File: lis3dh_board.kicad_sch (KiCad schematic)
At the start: 11 parts, among them J1 T4_I2C2, J2 BQ25798_BOARD, U1 TLV75530PDBV, U2 LIS3DH

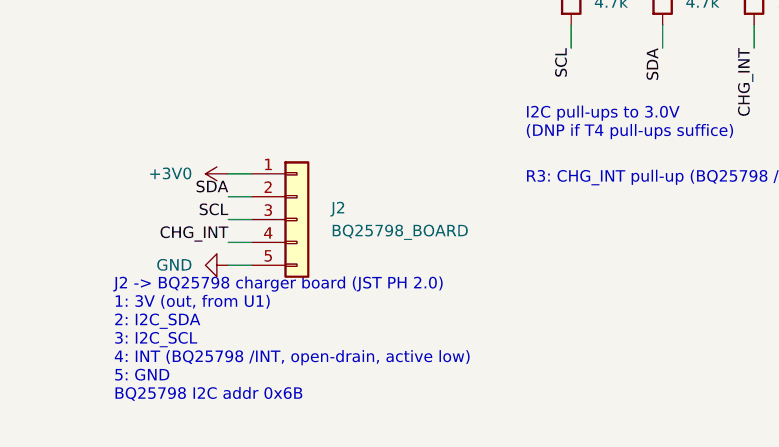
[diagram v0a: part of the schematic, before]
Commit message: Reverse J2 pin order for the charger board connector
J2 (JST PH 2.0 to the BQ25798 board) is now 1 GND, 2 INT, 3 SCL,
4 SDA, 5 3V. Nets are unchanged; only the pin numbering is reversed.

Co-Authored-By: Claude Opus 5.5 <noreply@anthropic.com>
Claude-Session: https://claude.ai/code/session_012K15v8QNdkAoa4NiCNiWuG
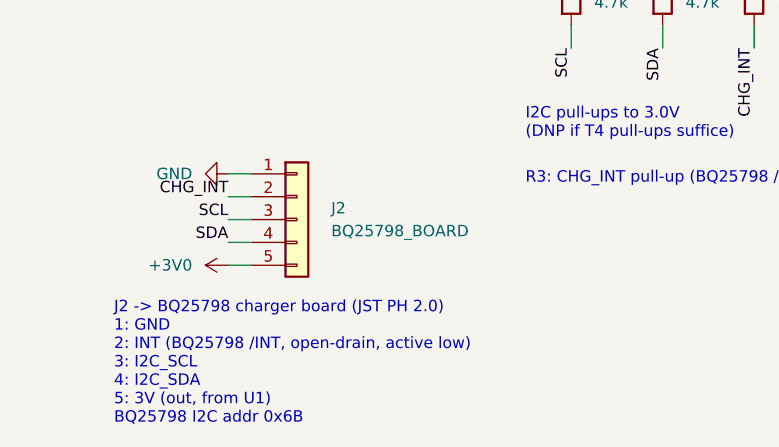
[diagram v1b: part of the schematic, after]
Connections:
- net +3V0: now also J2.5 (Pin_5); no longer J2.1 (Pin_1)
- net CHG_INT: now also J2.2 (Pin_2); no longer J2.4 (Pin_4)
- net GND: now also J2.1 (Pin_1); no longer J2.5 (Pin_5)
- net SDA: now also J2.4 (Pin_4); no longer J2.2 (Pin_2)
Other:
- note added: "J2 -> BQ25798 charger board (JST PH 2.0) 1: GND 2: INT (BQ25798 /INT, open-drain, active low) 3: I2C_SCL 4: I2C_SDA 5: 3V (out, from U1) BQ25798 I2C addr 0x6B"
- note removed: "J2 -> BQ25798 charger board (JST PH 2.0) 1: 3V (out, from U1) 2: I2C_SDA 3: I2C_SCL 4: INT (BQ25798 /INT, open-drain, active low) 5: GND BQ25798 I2C addr 0x6B"
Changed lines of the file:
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@@
     (stroke (width 0) (type default))
   )
-  (symbol (lib_id "power:+3V0") (at 43.18 137.16 90) (unit 1)
+  (symbol (lib_id "power:GND") (at 43.18 137.16 270) (unit 1)
     (in_bom no) (on_board no) (dnp no)
     (property "Reference" "#PWR016" (at 43.18 143.16 0)
       (effects (font (size 1.27 1.27)) hide)
     )
-    (property "Value" "+3V0" (at 39.18 137.16 90)
+    (property "Value" "GND" (at 39.18 137.16 270)
       (effects (font (size 1.27 1.27)) (justify left))
     )
@@
     (stroke (width 0) (type default))
   )
-  (label "SDA" (at 43.18 139.7 180) (fields_autoplaced)
+  (label "CHG_INT" (at 43.18 139.7 180) (fields_autoplaced)
     (effects (font (size 1.27 1.27)) (justify right bottom))
   )
@@
     (stroke (width 0) (type default))
   )
-  (label "CHG_INT" (at 43.18 144.78 180) (fields_autoplaced)
+  (label "SDA" (at 43.18 144.78 180) (fields_autoplaced)
     (effects (font (size 1.27 1.27)) (justify right bottom))
   )
@@
     (stroke (width 0) (type default))
   )
-  (symbol (lib_id "power:GND") (at 43.18 147.32 270) (unit 1)
+  (symbol (lib_id "power:+3V0") (at 43.18 147.32 90) (unit 1)
     (in_bom no) (on_board no) (dnp no)
     (property "Reference" "#PWR017" (at 43.18 153.32 0)
       (effects (font (size 1.27 1.27)) hide)
     )
-    (property "Value" "GND" (at 39.18 147.32 270)
+    (property "Value" "+3V0" (at 39.18 147.32 90)
       (effects (font (size 1.27 1.27)) (justify left))
     )
@@
     )
   )
-  (text "J2 -> BQ25798 charger board (JST PH 2.0)\n1: 3V (out, from U1)\n2: I2C_SDA\n3: I2C_SCL\n4: INT (BQ25798 /INT, open-drain, active low)\n5: GND\nBQ25798 I2C addr 0x6B" (at 30.48 162.56 0)
+  (text "J2 -> BQ25798 charger board (JST PH 2.0)\n1: GND\n2: INT (BQ25798 /INT, open-drain, active low)\n3: I2C_SCL\n4: I2C_SDA\n5: 3V (out, from U1)\nBQ25798 I2C addr 0x6B" (at 30.48 165.1 0)
     (effects (font (size 1.27 1.27)) (justify left bottom))
   )

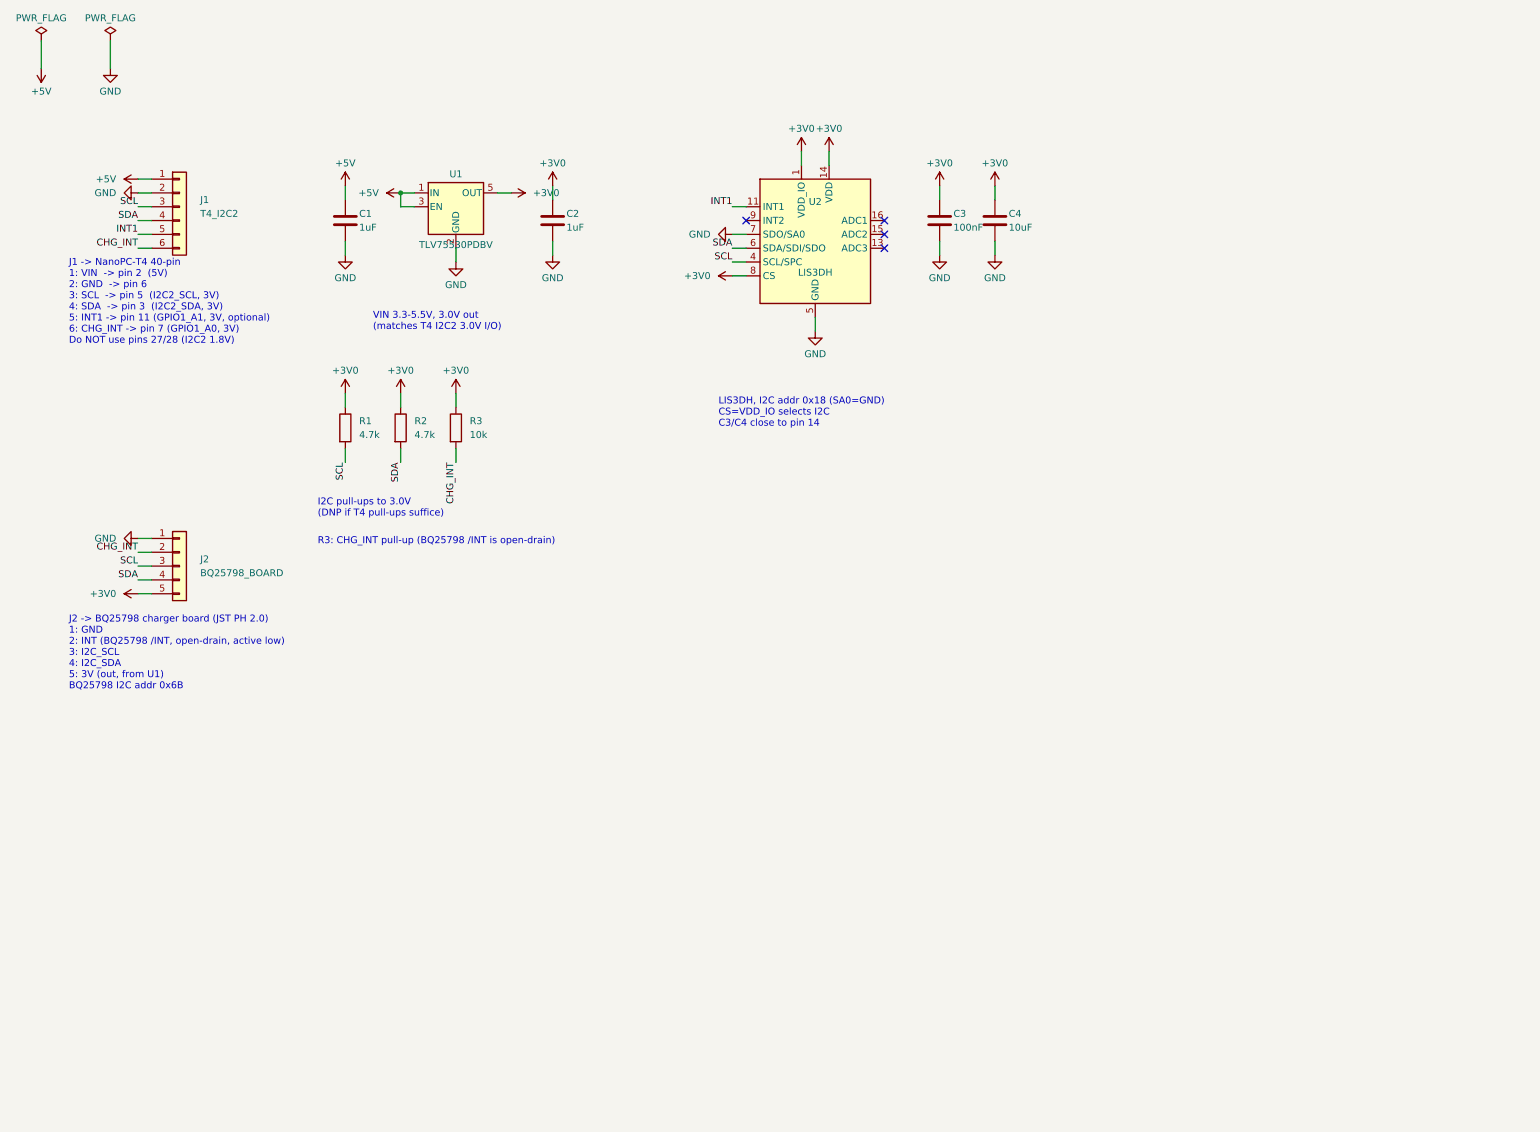
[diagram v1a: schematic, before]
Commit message: Add WL-125 125kHz RFID module socket
J3 is a 1x10 socket for the WL-125 (module pins 1-9, pin 10 is the
polarization key). The module runs from a filtered 5V rail (2.2R +
1000uF + 100nF, as its datasheet asks for clean power), pin 3 is tied
high for UART output, and its 5V TX is divided down to ~3.0V and sent
to T4 UART4_RX through new J1 pin 7. Antenna pins are left unconnected
since the coil is soldered on the module.

Co-Authored-By: Claude Opus 5.5 <noreply@anthropic.com>
Claude-Session: https://claude.ai/code/session_012K15v8QNdkAoa4NiCNiWuG
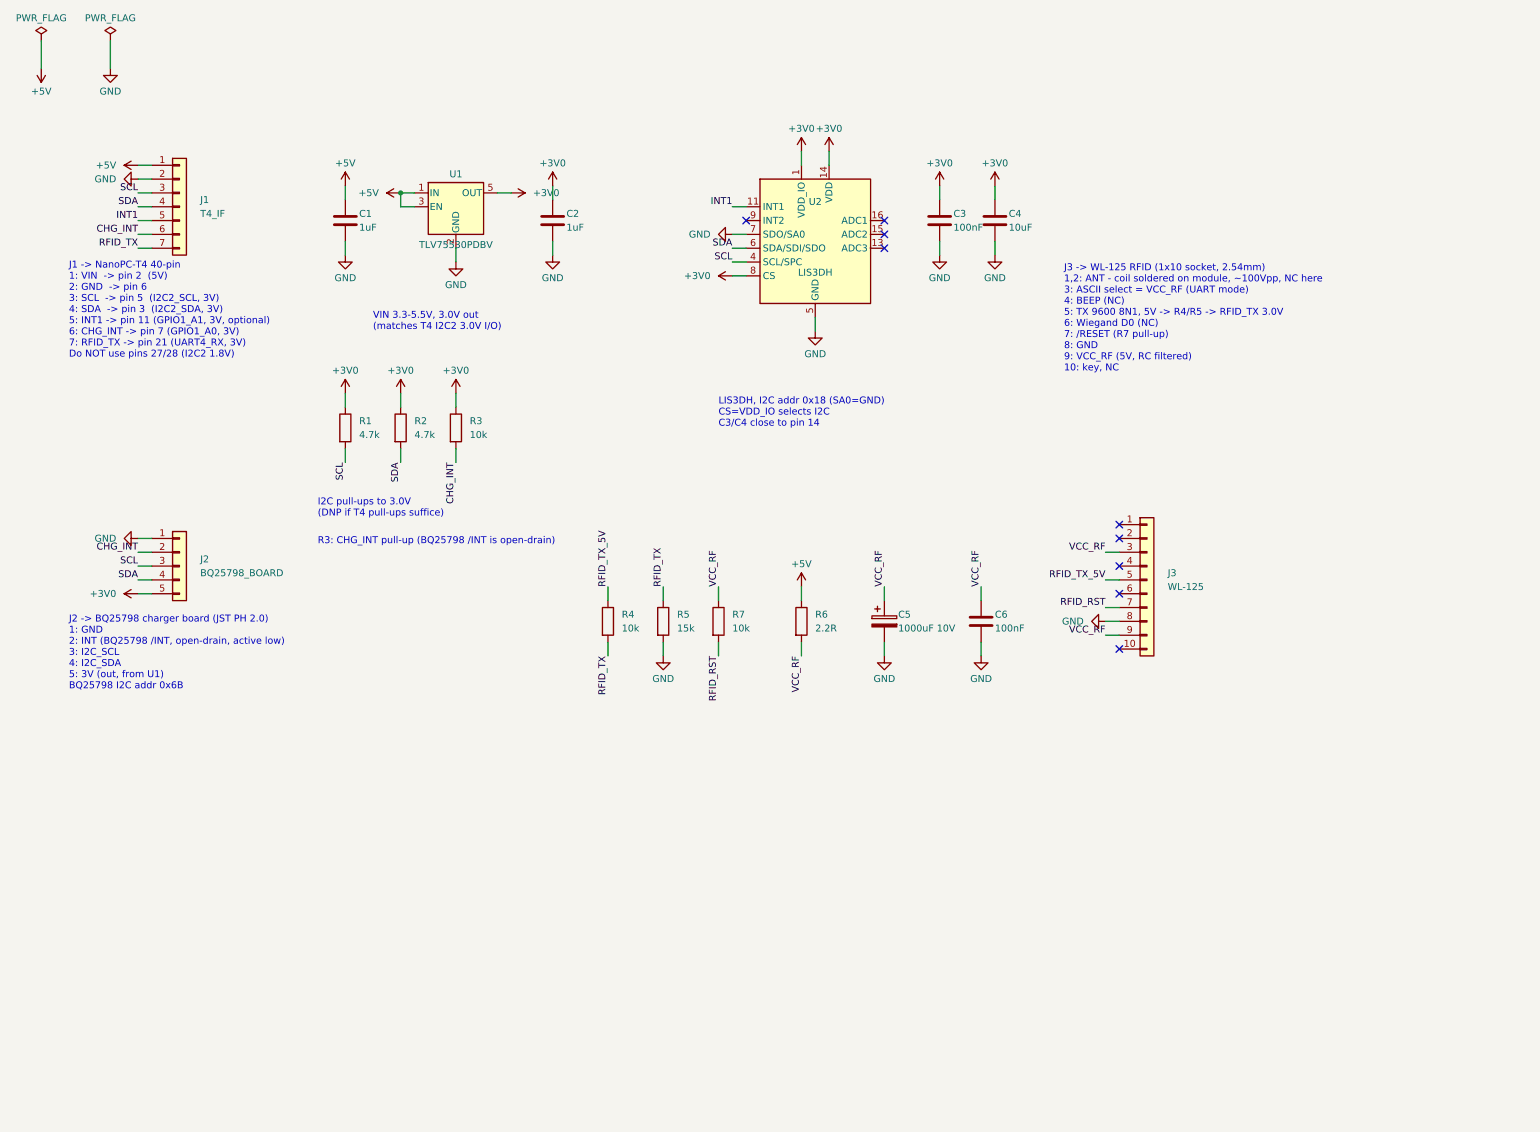
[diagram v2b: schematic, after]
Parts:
- removed J1: T4_I2C2, Connector_PinHeader_2.54mm:PinHeader_1x06_P2.54mm_Vertical, symbol Connector_Generic:Conn_01x06
- added C5: 1000uF 10V, Capacitor_THT:CP_Radial_D10.0mm_P5.00mm, symbol Device:C_Polarized
- added C6: 100nF, Capacitor_SMD:C_0603_1608Metric, symbol Device:C
- added J1: T4_IF, Connector_PinHeader_2.54mm:PinHeader_1x07_P2.54mm_Vertical, symbol Connector_Generic:Conn_01x07
- added J3: WL-125, Connector_PinSocket_2.54mm:PinSocket_1x10_P2.54mm_Vertical, symbol Connector_Generic:Conn_01x10
- added R4, R7: 10k, Resistor_SMD:R_0603_1608Metric, symbol Device:R
- added R5: 15k, Resistor_SMD:R_0603_1608Metric, symbol Device:R
- added R6: 2.2R, Resistor_SMD:R_0805_2012Metric, symbol Device:R
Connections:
- net +5V: now also J1.1 (Pin_1), R6.1
- net CHG_INT: now also J1.6 (Pin_6)
- net GND: now also C5.2, C6.2, J1.2 (Pin_2), J3.8 (Pin_8), R5.2
- net INT1: now also J1.5 (Pin_5)
- net SCL: now also J1.3 (Pin_3)
- net SDA: now also J1.4 (Pin_4)
- new net RFID_RST: J3.7 (Pin_7), R7.2
- new net RFID_TX: J1.7 (Pin_7), R4.2, R5.1
- new net RFID_TX_5V: J3.5 (Pin_5), R4.1
- new net VCC_RF: C5.1, C6.1, J3.3 (Pin_3), J3.9 (Pin_9), R6.2, R7.1
- no-connect marks 4 -> 9
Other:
- note added: "J1 -> NanoPC-T4 40-pin 1: VIN -> pin 2 (5V) 2: GND -> pin 6 3: SCL -> pin 5 (I2C2_SCL, 3V) 4: SDA -> pin 3 (I2C2_SDA, 3V) 5: INT1 -> pin 11 (GPIO1_A1, 3V, optional) 6: CHG_INT -> pin 7 (GPIO1_A0, 3V) 7: RFID_TX -> pin 21 (UART4_RX, 3V) Do NOT use pins 27/28 (I2C2 1.8V)"
- note added: "J3 -> WL-125 RFID (1x10 socket, 2.54mm) 1,2: ANT - coil soldered on module, ~100Vpp, NC here 3: ASCII select = VCC_RF (UART mode) 4: BEEP (NC) 5: TX 9600 8N1, 5V -> R4/R5 -> RFID_TX 3.0V 6: Wiegand D0 (NC) 7: /RESET (R7 pull-up) 8: GND 9: VCC_RF (5V, RC filtered) 10: key, NC"
- note removed: "J1 -> NanoPC-T4 40-pin 1: VIN -> pin 2 (5V) 2: GND -> pin 6 3: SCL -> pin 5 (I2C2_SCL, 3V) 4: SDA -> pin 3 (I2C2_SDA, 3V) 5: INT1 -> pin 11 (GPIO1_A1, 3V, optional) 6: CHG_INT -> pin 7 (GPIO1_A0, 3V) Do NOT use pins 27/28 (I2C2 1.8V)"

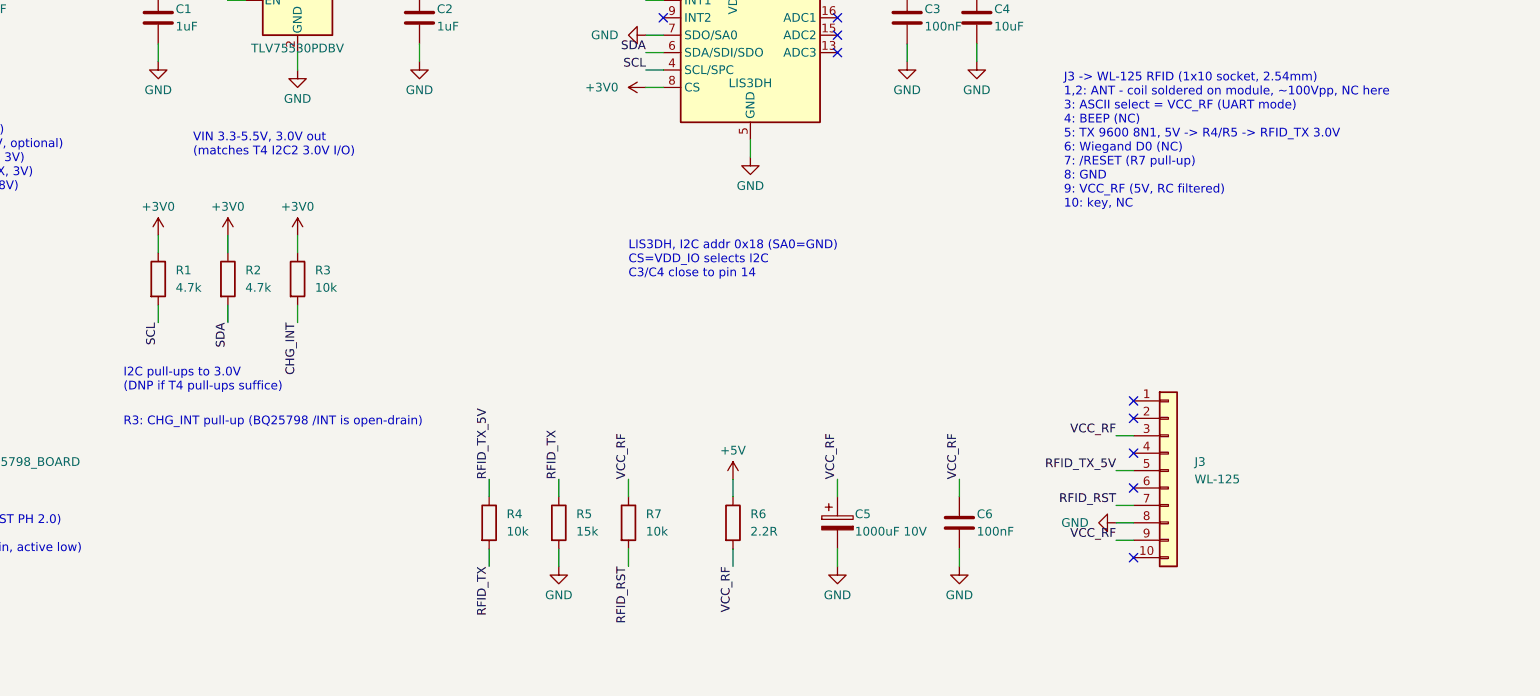
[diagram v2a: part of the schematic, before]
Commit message: Use a BSS138 level shifter for the WL-125 TX line
Replace the R4/R5 resistor divider with a BSS138 bidirectional level
shifter (Adafruit #757 topology): 10k pull-ups on the 3.0V and 5V sides,
gate tied to 3.0V.

Co-Authored-By: Claude Opus 5.5 <noreply@anthropic.com>
Claude-Session: https://claude.ai/code/session_012K15v8QNdkAoa4NiCNiWuG
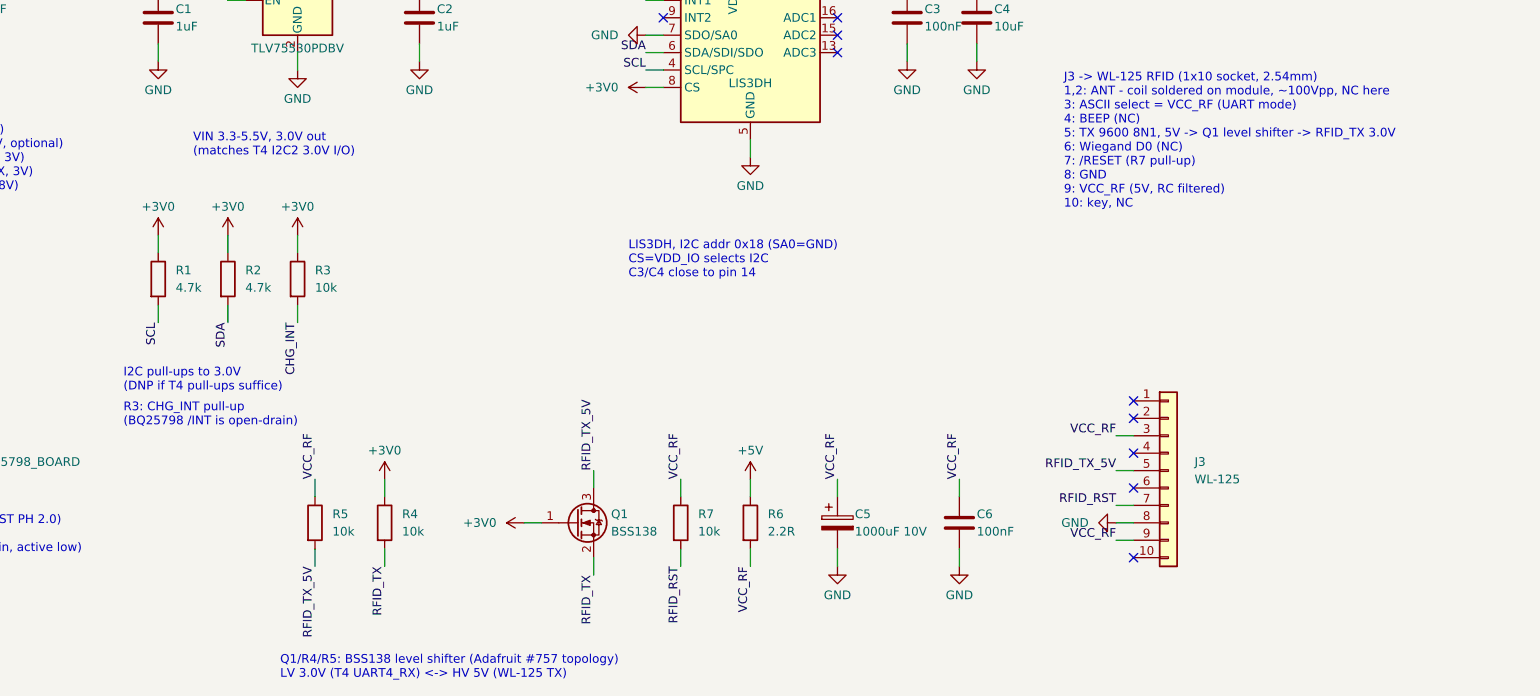
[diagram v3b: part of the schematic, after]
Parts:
- added Q1: BSS138, Package_TO_SOT_SMD:SOT-23, symbol Transistor_FET:BSS138
- R4: renamed from R5; value 15k -> 10k
- renumbered R4 to R5
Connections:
- net +3V0: now also R4.1, Q1.1 (G)
- net GND: no longer R4.2
- net RFID_TX: now also R4.2, Q1.2 (S); no longer R4.1, R5.2
- net RFID_TX_5V: now also R5.2, Q1.3 (D); no longer R5.1
- net VCC_RF: now also R5.1
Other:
- note added: "J3 -> WL-125 RFID (1x10 socket, 2.54mm) 1,2: ANT - coil soldered on module, ~100Vpp, NC here 3: ASCII select = VCC_RF (UART mode) 4: BEEP (NC) 5: TX 9600 8N1, 5V -> Q1 level shifter -> RFID_TX 3.0V 6: Wiegand D0 (NC) 7: /RESET (R7 pull-up) 8: GND 9: VCC_RF (5V, RC filtered) 10: key, NC"
- note added: "Q1/R4/R5: BSS138 level shifter (Adafruit #757 topology) LV 3.0V (T4 UART4_RX) <-> HV 5V (WL-125 TX)"
- note removed: "J3 -> WL-125 RFID (1x10 socket, 2.54mm) 1,2: ANT - coil soldered on module, ~100Vpp, NC here 3: ASCII select = VCC_RF (UART mode) 4: BEEP (NC) 5: TX 9600 8N1, 5V -> R4/R5 -> RFID_TX 3.0V 6: Wiegand D0 (NC) 7: /RESET (R7 pull-up) 8: GND 9: VCC_RF (5V, RC filtered) 10: key, NC"
- moved on the sheet: R4, R5
